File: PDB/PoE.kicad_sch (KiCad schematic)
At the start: 0 parts

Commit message: Add 24V@1.5A
Filled 24V@1.5A schem and added hierarchal pins to each sub sheet
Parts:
- added Cboot, Cinx: 100nF, symbol Device:C
- added Ccomp: 820pF, symbol Device:C
- added Ccomp2: 47nF, symbol Device:C
- added Cin: 15uF, symbol Device:C_US
- added Cout: 22uF, symbol Device:C_US
- added Coutx, Coutx2: 470nF, symbol Device:C
- added Cramp: 680pF, symbol Device:C
- added Css: 22nF, symbol Device:C
- added Cvcc: 1uF, symbol Device:C
- added D1: 850mV, symbol Device:D_Zener
- added D2: 950mV, symbol Device:D_Zener
- added L1: 33uH, symbol Device:L
- added Q1: CSD19502Q5B, foot:CSD19502Q5B, symbol sym&foot:CSD19502Q5B
- added Q2: CSD19502Q5B, CSD19502Q5B:TRANS_CSD19502Q5B, symbol sym&foot:CSD19502Q5B
- added Rcomp: 12.1kOhm, symbol Device:R
- added Renable: 1MOhm, symbol Device:R
- added Rfbb: 1kOhm, symbol Device:R
- added Rfbt, Rt: 18.7kOhm, symbol Device:R
- added Rramp: 105kOhm, symbol Device:R
- added Rsense: 25mOhm, symbol Device:R
- added Ruv1: 64.9kOhm, symbol Device:R
- added Ruv2: 10kOhm, symbol Device:R
- added U5: LM5118MH, foot:LM5118MH, symbol sym&foot:LM5118MH
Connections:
- new net: Cboot.1, D1.1 (K), L1.1, Q1.1, Q1.2, Q1.3, U5.20 (HS)
- new net: D2.2 (A), L1.2, Q2.5_8
- new net: Ccomp.2, Ccomp2.2, Rfbb.1, Rfbt.2, U5.8 (FB)
- new net: Ccomp.1, Rcomp.1, U5.9 (COMP)
- new net: Ccomp2.1, Rcomp.2
- new net: Ruv1.2, Ruv2.1, U5.2 (UVLO)
- new net: D1.2 (A), Rsense.1, U5.12 (CS)
- new net: Q2.4, U5.15 (LO)
- new net: Cvcc.1, Rramp.1, U5.16 (VCC)
- new net: Cboot.2, U5.18 (HB)
- new net: Q1.4, U5.19 (HO)
- new net: Rt.1, U5.3 (RT)
- new net: Renable.2, U5.4 (EN)
- new net: Cramp.1, Rramp.2, U5.5 (RAMP)
- new net: Css.1, U5.7 (SS)
- new net +BATT: Cin.1, Cinx.1, Q1.5_8, Renable.1, Ruv1.1, U5.1 (VIN)
- new net 24V@1.5A: Cout.1, Coutx.1, Coutx2.1, D2.1 (K), Rfbt.1, U5.10 (VOUT)
- new net GND: Cin.2, Cinx.2, Cout.2, Coutx.2, Coutx2.2, Cramp.2, Css.2, Cvcc.2, Q2.1, Q2.2, Q2.3, Rfbb.2, Rsense.2, Rt.2, Ruv2.2, U5.13 (CSG), U5.14 (PGND), U5.17 (VCCX), U5.6 (AGND)
- no-connect marks 0 -> 1

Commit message: added fuses to each
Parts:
- added F3: TR/3216FF15-R, symbol Device:Fuse
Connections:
- net 24V@1.5A: now also F3.1, F3.2
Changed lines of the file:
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@@
 	)
 	(junction
-		(at 44.45 45.72)
+		(at 271.78 81.28)
 		(diameter 0)
 		(color 0 0 0 0)
 	)
 	(junction
-		(at 190.5 113.03)
+		(at 44.45 45.72)
 		(diameter 0)
 		(color 0 0 0 0)
 	)
 	(junction
-		(at 190.5 76.2)
+		(at 190.5 113.03)
 		(diameter 0)
 		(color 0 0 0 0)
 	)
 	(junction
-		(at 271.78 81.28)
+		(at 190.5 76.2)
 		(diameter 0)
 		(color 0 0 0 0)
@@
 	(wire
 		(pts
+			(xy 271.78 78.74) (xy 271.78 81.28)
+		)
+		(stroke
+			(width 0)
+			(type default)
+		)
+	)
+	(wire
+		(pts
 			(xy 110.49 102.87) (xy 110.49 114.3)
 		)
@@
 	(wire
 		(pts
+			(xy 271.78 68.58) (xy 271.78 71.12)
+		)
+		(stroke
+			(width 0)
+			(type default)
+		)
+	)
+	(wire
+		(pts
 			(xy 256.54 100.33) (xy 256.54 113.03)
 		)
@@
 	(symbol
 		(lib_id "power:+1V5")
-		(at 271.78 81.28 0)
+		(at 271.78 68.58 0)
 		(unit 1)
 		(body_style 1)
@@
 		(fields_autoplaced yes)
 		(property "Reference" "#PWR021"
-			(at 271.78 85.09 0)
+			(at 271.78 72.39 0)
 			(hide yes)
 			(show_name no)
@@
 		)
 		(property "Value" "24V@1.5A"
-			(at 271.78 76.2 0)
+			(at 271.78 63.5 0)
 			(show_name no)
 			(do_not_autoplace no)
@@
 		)
 		(property "Footprint" ""
-			(at 271.78 81.28 0)
+			(at 271.78 68.58 0)
 			(hide yes)
 			(show_name no)
@@
 		)
 		(property "Datasheet" ""
-			(at 271.78 81.28 0)
+			(at 271.78 68.58 0)
 			(hide yes)
 			(show_name no)
@@
 		)
 		(property "Description" "Power symbol creates a global label with name \"+1V5\""
-			(at 271.78 81.28 0)
+			(at 271.78 68.58 0)
 			(hide yes)
 			(show_name no)
@@
 					(unit 1)
 				)
+			)
+		)
+	)
+	(symbol
+		(lib_id "Device:Fuse")
+		(at 271.78 74.93 180)
+		(unit 1)
+		(body_style 1)
+		(exclude_from_sim no)
+		(in_bom yes)
+		(on_board yes)
+		(in_pos_files yes)
+		(dnp no)
+		(fields_autoplaced yes)
+		(property "Reference" "F3"
+			(at 274.32 73.6599 0)
+			(show_name no)
+			(do_not_autoplace no)
+			(effects
+				(font
+					(size 1.27 1.27)
+				)
+				(justify right)
+			)
+		)
+		(property "Value" "TR/3216FF15-R"
+			(at 274.32 76.1999 0)
+			(show_name no)
+			(do_not_autoplace no)
+			(effects
+				(font
+					(size 1.27 1.27)
+				)
+				(justify right)
+			)
+		)
+		(property "Footprint" ""
+			(at 273.558 74.93 90)
+			(hide yes)
+			(show_name no)
+			(do_not_autoplace no)
+			(effects
+				(font
+					(size 1.27 1.27)
+				)
+			)
+		)
+		(property "Datasheet" ""
+			(at 271.78 74.93 0)
+			(hide yes)
+			(show_name no)
+			(do_not_autoplace no)
+			(effects
+				(font
+					(size 1.27 1.27)
+				)
+			)
+		)
+		(property "Description" "Fuse"
+			(at 271.78 74.93 0)
+			(hide yes)
+			(show_name no)
+			(do_not_autoplace no)
+			(effects
+				(font
+					(size 1.27 1.27)
+				)
+			)
+		)
+		(pin "2"
+		)
+		(pin "1"
+		)
+		(instances
+			(project "PDB"
+				(path "/a9cf05c4-aac5-4cf1-b700-1d3045f8dfbd/73280642-a7d9-4144-aaf4-80e2ae791ad9"
+					(reference "F3")
+					(unit 1)
+				)

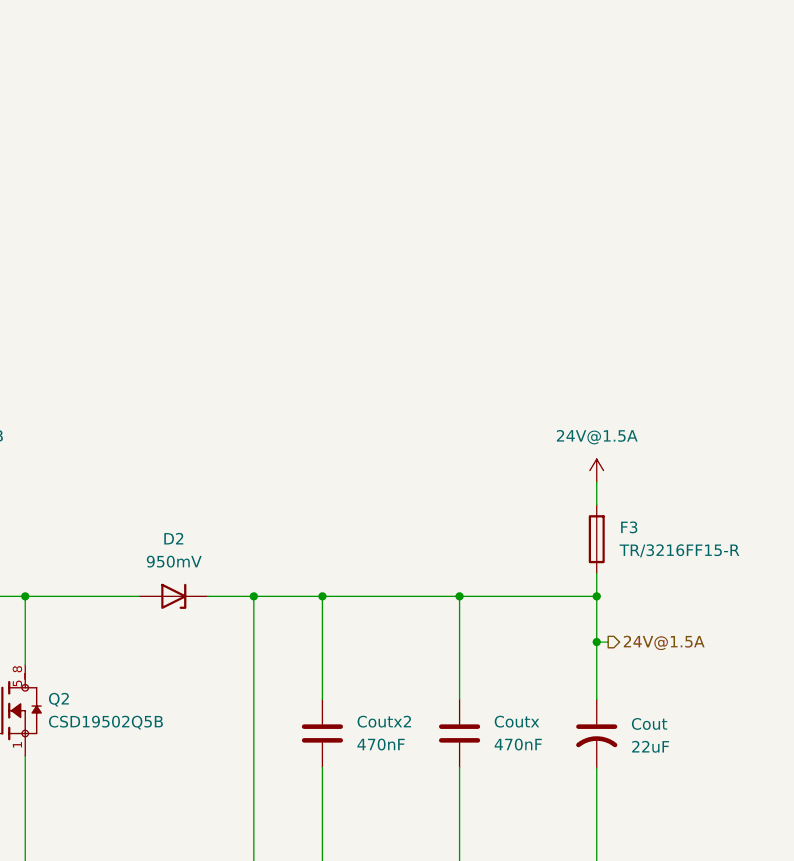
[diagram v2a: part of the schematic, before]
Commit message: added temp sensing on every rail available
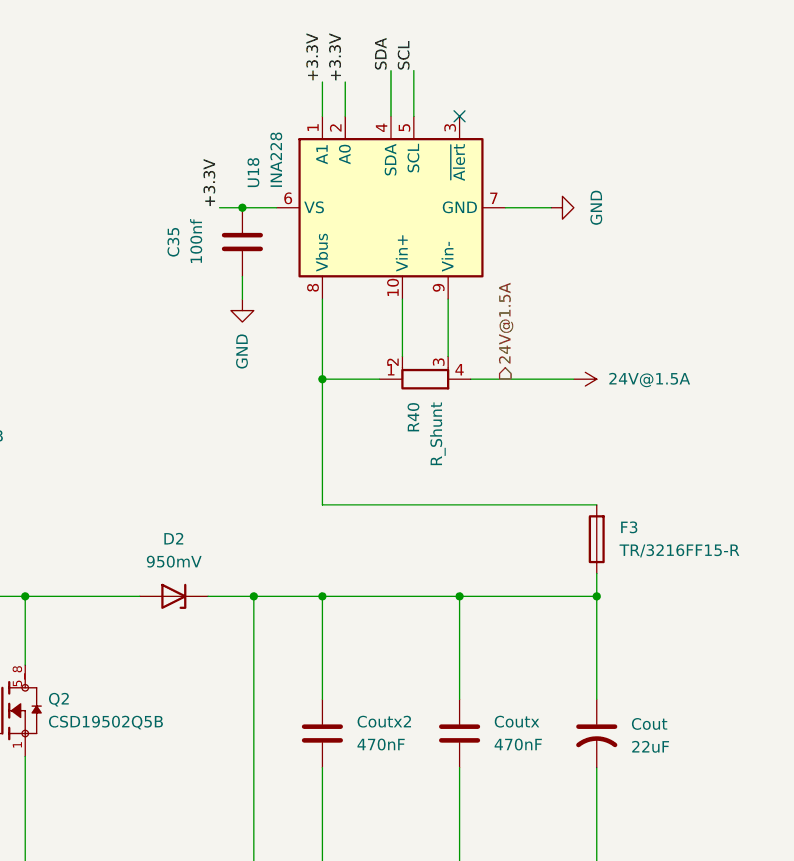
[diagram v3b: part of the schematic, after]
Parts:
- added C35: 100nf, Capacitor_SMD:C_1206_3216Metric, symbol Device:C
- added R40: R_Shunt, symbol Device:R_Shunt
- added U18: INA228, Package_SO:TSSOP-10_3x3mm_P0.5mm, symbol Sensor_Energy:INA228
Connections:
- net 24V@1.5A: now also R40.4; no longer Cout.1, Coutx.1, Coutx2.1, D2.1 (K), F3.1, F3.2, Rfbt.1, U5.10 (VOUT)
- net GND: now also C35.1, U18.7 (GND)
- new net: Cout.1, Coutx.1, Coutx2.1, D2.1 (K), F3.1, Rfbt.1, U5.10 (VOUT)
- new net: F3.2, R40.1, U18.8 (Vbus)
- new net: R40.2, U18.10 (Vin+)
- new net: R40.3, U18.9 (Vin-)
- new net +3.3V: C35.2, U18.1 (A1), U18.2 (A0), U18.6 (VS)
- new net SCL: U18.5 (SCL)
- new net SDA: U18.4 (SDA)
- no-connect marks 1 -> 2

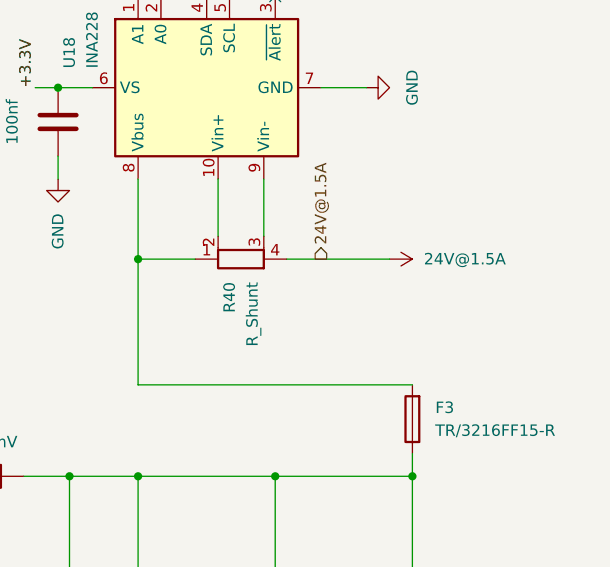
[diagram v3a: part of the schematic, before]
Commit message: added tp's, switches, inputs/outputs
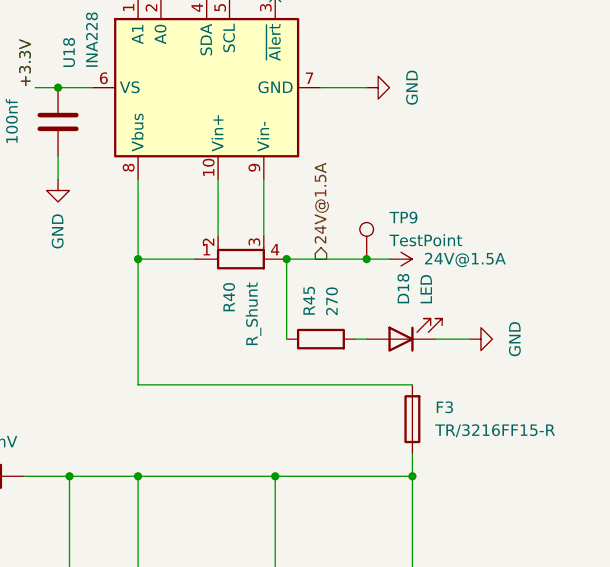
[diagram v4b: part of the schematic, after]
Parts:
- added D18: LED, LED_SMD:LED_0805_2012Metric, symbol Device:LED
- added R45: 270, Resistor_SMD:R_1206_3216Metric_Pad1.30x1.75mm_HandSolder, symbol Device:R
- added TP9: TestPoint, TestPoint:TestPoint_Pad_D2.0mm, symbol Connector:TestPoint
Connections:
- net 24V@1.5A: now also R45.1, TP9.1
- net GND: now also D18.1 (K)
- new net: D18.2 (A), R45.2

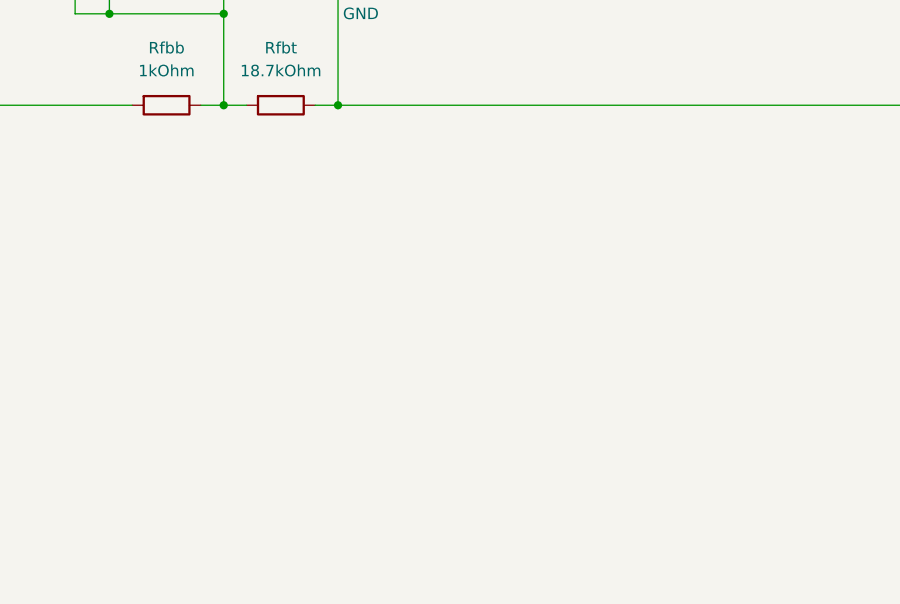
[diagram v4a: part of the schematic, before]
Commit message: added RJ45 in PoE sch
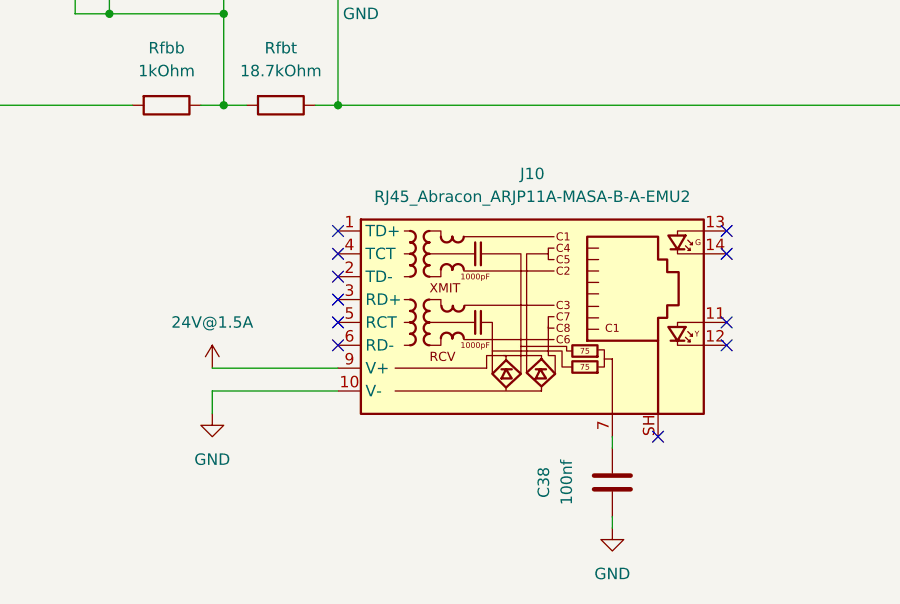
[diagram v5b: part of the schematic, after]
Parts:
- added C38: 100nf, Capacitor_SMD:C_1206_3216Metric, symbol Device:C
- added J10: RJ45_Abracon_ARJP11A-MASA-B-A-EMU2, Connector_RJ:RJ45_Abracon_ARJP11A-MA_Horizontal, symbol Connector:RJ45_Abracon_ARJP11A-MASA-B-A-EMU2
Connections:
- net 24V@1.5A: now also J10.9 (V+)
- net GND: now also C38.1, J10.10 (V-)
- new net: C38.2, J10.7
- no-connect marks 2 -> 13

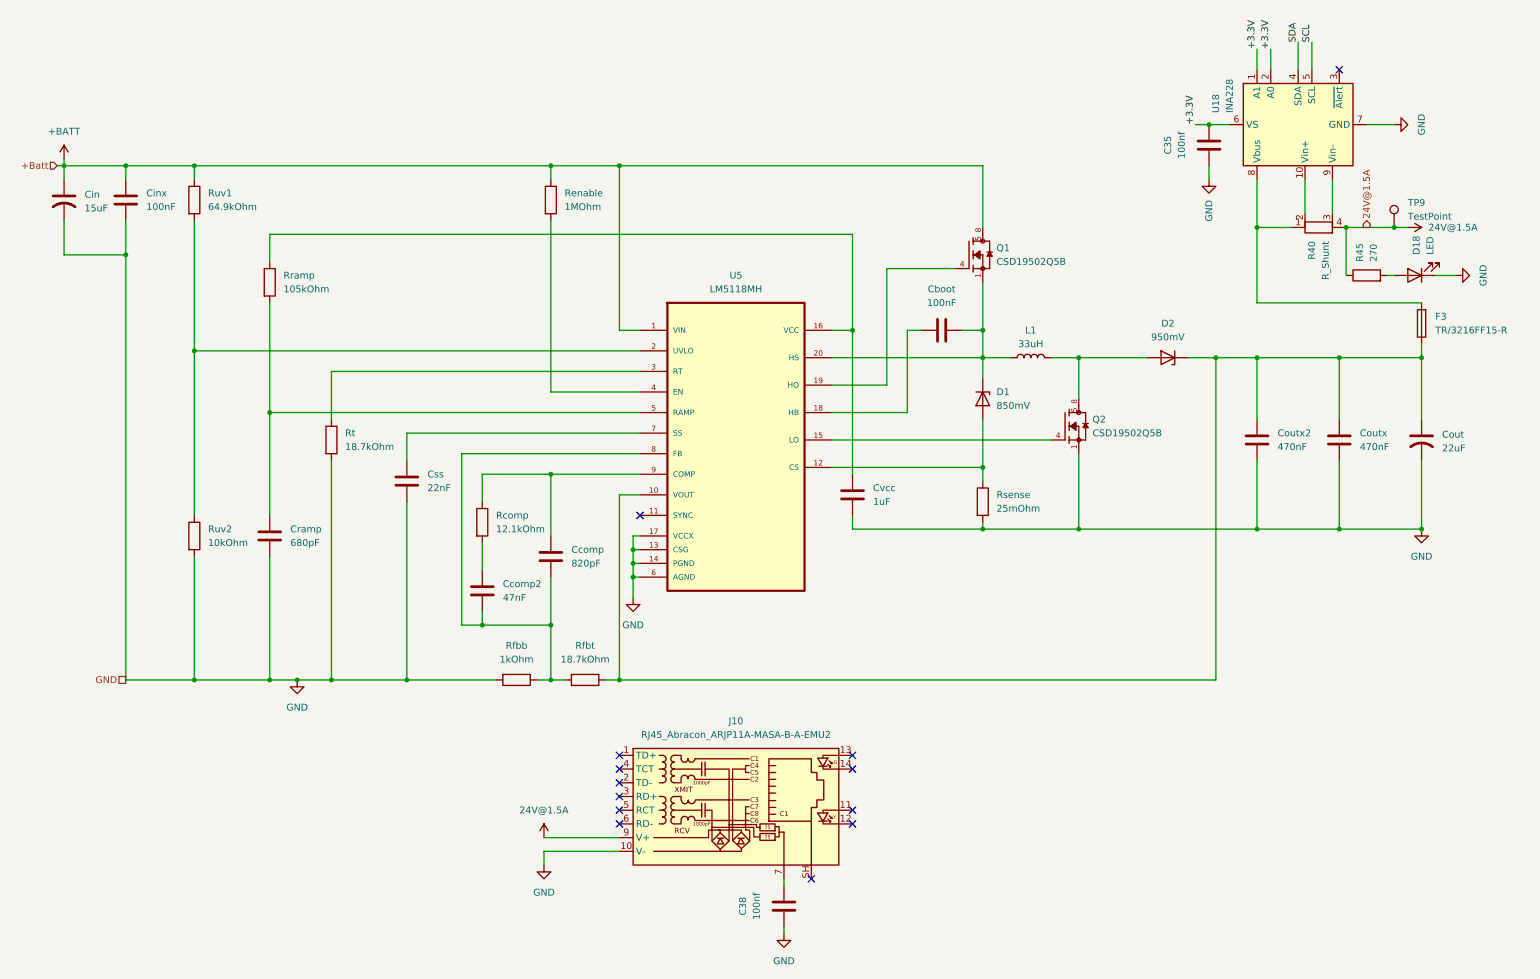
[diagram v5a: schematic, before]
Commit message: Finished all the footprints. doing poe myself now
finally.
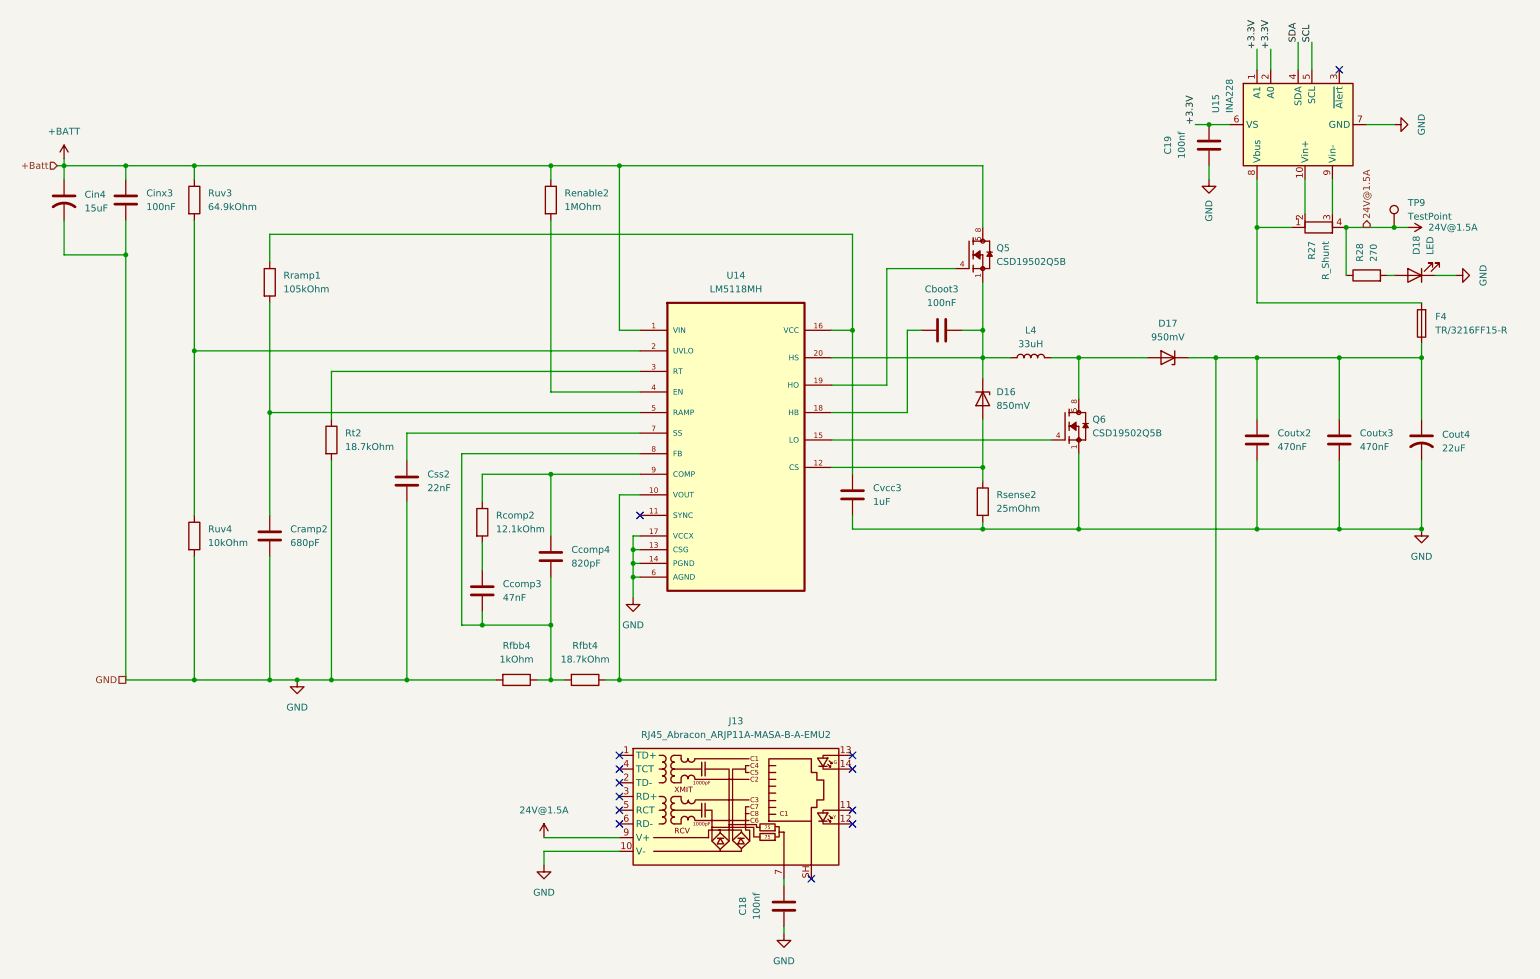
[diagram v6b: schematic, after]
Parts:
- C18: renamed from C38; footprint Capacitor_SMD:C_1206_3216Metric -> Capacitor_SMD:C_0603_1608Metric
- C19: renamed from C35; footprint Capacitor_SMD:C_1206_3216Metric -> Capacitor_SMD:C_0603_1608Metric
- Cboot3: renamed from Cboot; footprint (none) -> Capacitor_SMD:C_0603_1608Metric
- Ccomp3: renamed from Ccomp2; footprint (none) -> Capacitor_SMD:C_0603_1608Metric
- Ccomp4: renamed from Ccomp; footprint (none) -> Capacitor_SMD:C_0603_1608Metric
- Cin4: renamed from Cin; footprint (none) -> Capacitor_SMD:C_0603_1608Metric
- Cinx3: renamed from Cinx; footprint (none) -> Capacitor_SMD:C_0603_1608Metric
- Cout4: renamed from Cout; footprint (none) -> Capacitor_SMD:C_0603_1608Metric
- Coutx2: footprint (none) -> Capacitor_SMD:C_0603_1608Metric
- Coutx3: renamed from Coutx; footprint (none) -> Capacitor_SMD:C_0603_1608Metric
- Cramp2: renamed from Cramp; footprint (none) -> Capacitor_SMD:C_0603_1608Metric
- Css2: renamed from Css; footprint (none) -> Capacitor_SMD:C_0603_1608Metric
- Cvcc3: renamed from Cvcc; footprint (none) -> Capacitor_SMD:C_0603_1608Metric
- D16: renamed from D1; footprint (none) -> Diode_SMD:D_SOD-523
- D17: renamed from D2; footprint (none) -> Diode_SMD:D_SOD-523
- F4: renamed from F3; footprint (none) -> Fuse:Fuse_1206_3216Metric
- L4: renamed from L1; footprint (none) -> Inductor_SMD:L_1206_3216Metric
- R27: renamed from R40; footprint (none) -> Resistor_SMD:R_0603_1608Metric
- Rcomp2: renamed from Rcomp; footprint (none) -> Resistor_SMD:R_0603_1608Metric
- Renable2: renamed from Renable; footprint (none) -> Resistor_SMD:R_0603_1608Metric
- Rfbb4: renamed from Rfbb; footprint (none) -> Resistor_SMD:R_0603_1608Metric
- Rfbt4: renamed from Rfbt; footprint (none) -> Resistor_SMD:R_0603_1608Metric
- Rramp1: renamed from Rramp; footprint (none) -> Resistor_SMD:R_0603_1608Metric
- Rsense2: renamed from Rsense; footprint (none) -> Resistor_SMD:R_0603_1608Metric
- Rt2: renamed from Rt; footprint (none) -> Resistor_SMD:R_0603_1608Metric
- Ruv3: renamed from Ruv1; footprint (none) -> Resistor_SMD:R_0603_1608Metric
- Ruv4: renamed from Ruv2; footprint (none) -> Resistor_SMD:R_0603_1608Metric
- U15: renamed from U18; footprint Package_SO:TSSOP-10_3x3mm_P0.5mm -> Package_SO:HVSSOP-10-1EP_3x3mm_P0.5mm_EP1.83x1.89mm
- renumbered J10 to J13, Q1 to Q5, Q2 to Q6, R45 to R28, U5 to U14

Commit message: more footprint
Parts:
- Q5: footprint foot:CSD19502Q5B -> Dependencies:CSD19502Q5B
- Q6: footprint CSD19502Q5B:TRANS_CSD19502Q5B -> Dependencies:CSD19502Q5B
- U14: footprint foot:LM5118MH -> Dependencies:LM5118MH
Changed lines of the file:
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@@
 			)
 		)
-		(property "Footprint" "foot:LM5118MH"
+		(property "Footprint" "Dependencies:LM5118MH"
 			(at 144.78 93.98 0)
 			(hide yes)
@@
 			)
 		)
-		(property "Footprint" "CSD19502Q5B:TRANS_CSD19502Q5B"
+		(property "Footprint" "Dependencies:CSD19502Q5B"
 			(at 208.28 93.98 0)
 			(hide yes)
@@
 			)
 		)
-		(property "Footprint" "foot:CSD19502Q5B"
+		(property "Footprint" "Dependencies:CSD19502Q5B"
 			(at 190.5 62.23 0)
 			(hide yes)
